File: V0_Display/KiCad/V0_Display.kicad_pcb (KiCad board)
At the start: 2 copper layers, 80 x 35 mm, 31 parts, among them J1 USB_B_Micro, J2 I2C Header 1, J3 Conn_01x03, J4 Conn_01x02, J5 SWD Header, J6 I2C Header 2, J7 USB_Header, J8 Conn_01x02, SW1 SW_SPST, SW2 SW_SPST, SW3 SW_SPST, SW4 SW_SPST, SW5 SW_SPST, SW6 SW_SPST, SW7 Rotary_Encoder_Switch, U1 AP2127K-3.3, U2 STM32F042F6Px, U3 74LVC1G17

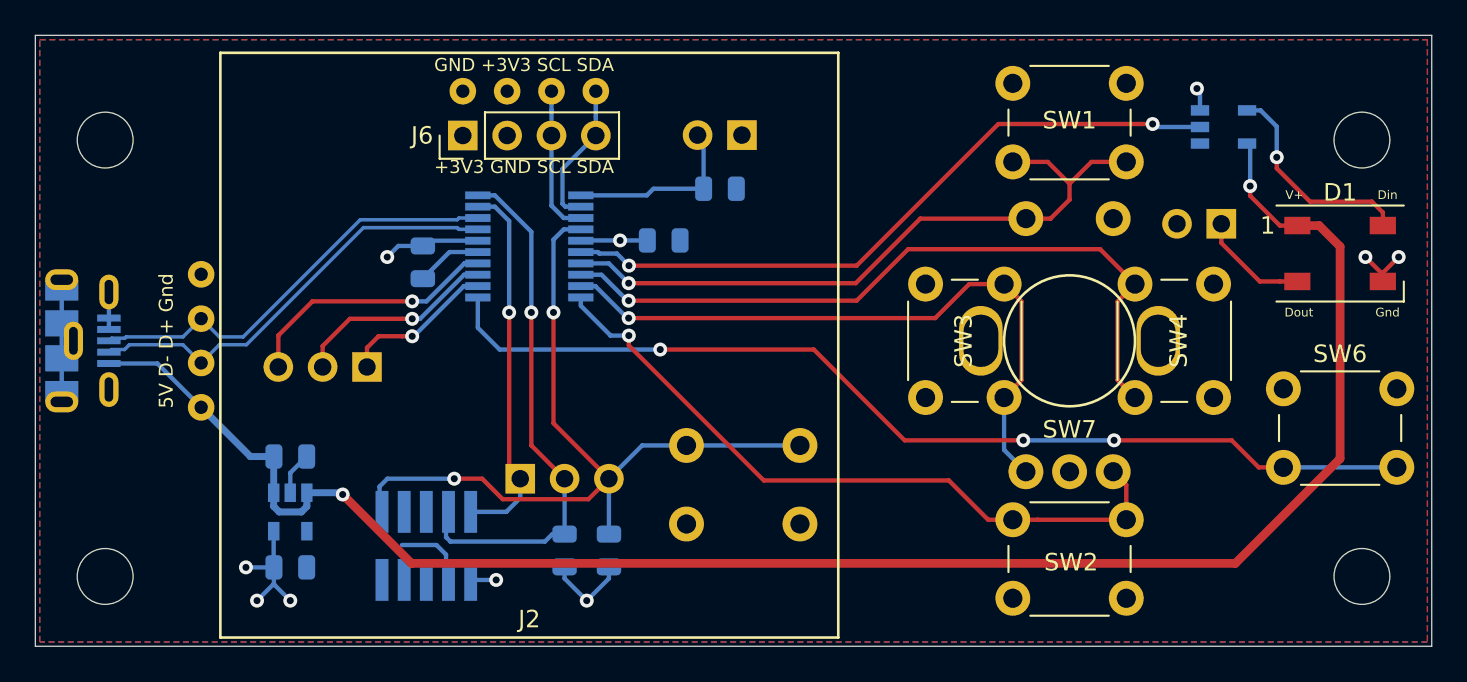
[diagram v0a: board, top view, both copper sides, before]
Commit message: Library Localization and Pinout changes
Added Selection jumpers for pins 1 and 2 on OLED header (Power and Ground) for use with different OLED pinouts.

Moved all footprints, schematic symbols and 3D models to the V0 folder for simplification
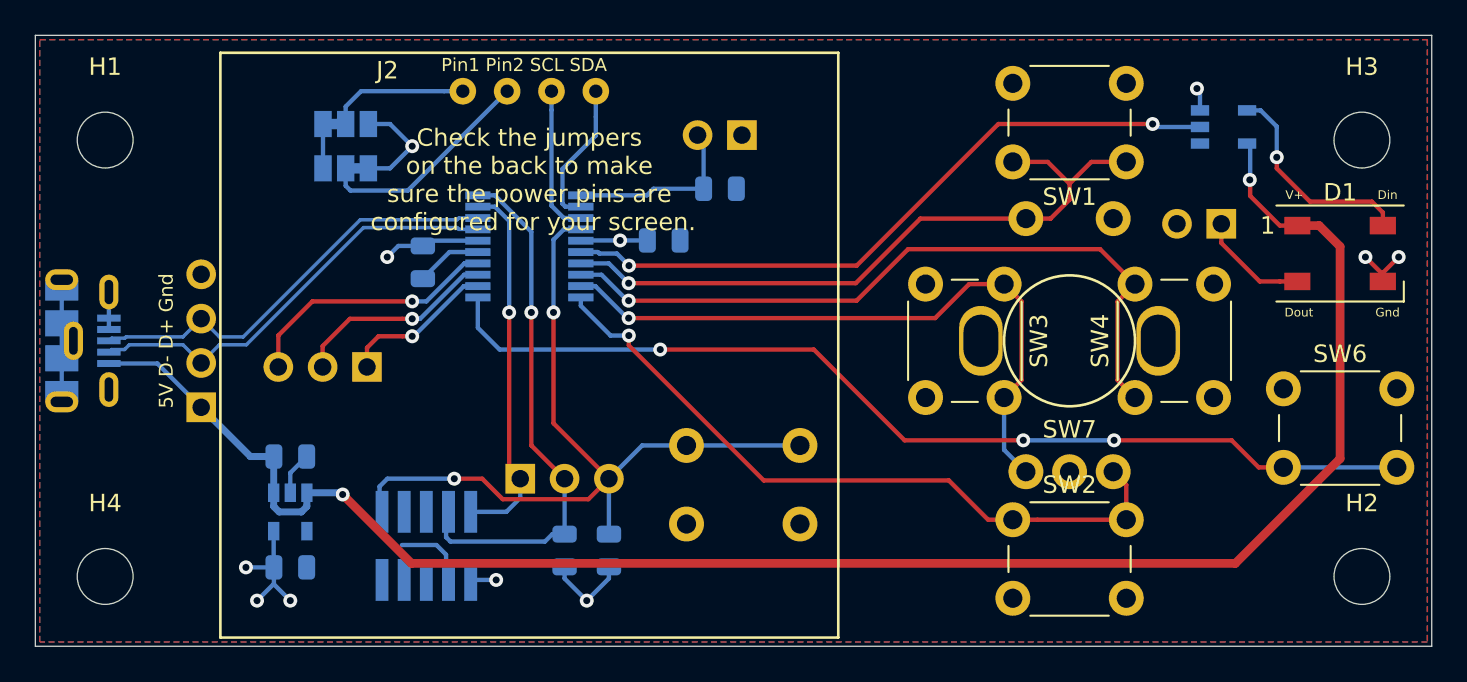
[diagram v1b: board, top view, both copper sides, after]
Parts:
- removed J6: I2C Header 2, Connector_PinHeader_2.54mm:PinHeader_1x04_P2.54mm_Vertical
- added JP1: Pin2, V0-Display:SolderJumper-3_P1.3mm_Bridged12_Pad1.0x1.5mm, B.Cu at (103.0, 57.3)
- added JP2: Pin1, V0-Display:SolderJumper-3_P1.3mm_Bridged12_Pad1.0x1.5mm, B.Cu at (103.0, 54.7)
- C1, C2, C3, C4: footprint Capacitor_SMD:C_0805_2012Metric -> V0-Display:C_0805_2012Metric
- D1: footprint LED_SMD:LED_WS2812B_PLCC4_5.0x5.0mm_P3.2mm -> V0-Display:LED_WS2812B_PLCC4_5.0x5.0mm_P3.2mm
- GPIO1: footprint Connector_PinHeader_2.54mm:PinHeader_1x03_P2.54mm_Horizontal -> V0-Display:PinHeader_1x03_P2.54mm_Vertical
- H1, H2, H3, H4: footprint MountingHole:MountingHole_3.2mm_M3 -> V0-Display:MountingHole_3.2mm_M3
- J1: footprint TRA_KiCad_Footprints:MolexVertical&Horizontal_MicroB -> V0-Display:MolexVertical&Horizontal_MicroB
- J2: footprint TRA_KiCad_Footprints:1pt3in_OLED -> V0-Display:1pt3in_OLED
- J3: footprint Connector_PinHeader_2.54mm:PinHeader_1x03_P2.54mm_Vertical -> V0-Display:PinHeader_1x03_P2.54mm_Vertical
- J4, J8: footprint Connector_PinHeader_2.54mm:PinHeader_1x02_P2.54mm_Vertical -> V0-Display:PinHeader_1x02_P2.54mm_Vertical
- J5: footprint Connector_PinHeader_1.27mm:PinHeader_2x05_P1.27mm_Vertical_SMD -> V0-Display:PinHeader_2x05_P1.27mm_Vertical_SMD
- J7: footprint TRA_KiCad_Footprints:01x04_unpopulated -> V0-Display:PinHeader_1x04_P2.54mm_Vertical
- R1, R2, R3: footprint Resistor_SMD:R_0805_2012Metric -> V0-Display:R_0805_2012Metric
- SW1, SW2, SW3, SW4: footprint Button_Switch_THT:SW_PUSH_6mm_H9.5mm -> V0-Display:SW_PUSH_6mm
- SW5, SW6: footprint Button_Switch_THT:SW_PUSH_6mm -> V0-Display:SW_PUSH_6mm
- SW7: footprint TRA_KiCad_Footprints:EN11_Encoder -> V0-Display:EN11_Encoder
- U1: footprint Package_TO_SOT_SMD:SOT-23-5 -> V0-Display:SOT-23-5
- U2: footprint Package_SO:TSSOP-20_4.4x6.5mm_P0.65mm -> V0-Display:TSSOP-20_4.4x6.5mm_P0.65mm
- U3: footprint digikey-footprints:SOT-753 -> V0-Display:SOT-753
- moved J7 3.81 mm to (94.7, 71.0), turned to 0 degrees
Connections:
- J2 pad 1: GND -> Pin1
- J2 pad 2: +3V3 -> Pin2
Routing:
- net Pin2: track 0.00 -> 12.7 mm
- net Pin1: track 0.00 -> 8.07 mm
- net +3V3: track 23.2 -> 29.3 mm, vias 7 -> 8
- net GND: track 26.2 -> 28.7 mm
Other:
- board text added: "1 2 3 GPIO"
- board text added: "1(GND)"
- board text added: "1(VCC)"
- board text added: "2(GND)"
- board text added: "2(VCC)"
- board text added: "Check the jumpers on the back to make sure the power pins are configured for your screen."
- board text added: "Neo-Out Gnd"
- board text added: "Pin1 Pin2 SCL SDA"
- board text added: "SDA SCL Pin2 Pin1"
- board text removed: "+3V3 GND SCL SDA"
- board text removed: "GND +3V3 SCL SDA"
- board text removed: "GPIO 1 2 3"
- board text removed: "SDA SCL +3V3 GND"
- board text removed: "SDA SCL GND +3V3"

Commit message: Add VORON logo and Rev number
Add Logo and Rev number
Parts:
- added G***: LOGO, V0-Display:VoronLogo_6pt5mm_silkScreen, B.Cu at (144.4, 67.2)
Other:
- board text added: "T. Abraham V0-Display Rev-C"
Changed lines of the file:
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@@
   (general
     (thickness 1.6)
-    (drawings 55)
+    (drawings 56)
     (tracks 280)
     (zones 0)
-    (modules 32)
+    (modules 33)
     (nets 25)
   )
@@
     (solder_mask_min_width 0.25)
     (aux_axis_origin 0 0)
-    (grid_origin 94.67 70.96)
+    (grid_origin 144.42 67.15)
     (visible_elements 7FFFFFFF)
     (pcbplotparams
@@
     (add_net "Net-(D1-Pad2)")
     (add_net "Net-(D1-Pad4)")
-    (add_net "Net-(GPIO1-Pad1)")
-    (add_net "Net-(GPIO1-Pad2)")
-    (add_net "Net-(J5-Pad6)")
-    (add_net "Net-(J5-Pad7)")
-    (add_net "Net-(J5-Pad8)")
-    (add_net "Net-(J5-Pad9)")
-    (add_net "Net-(U1-Pad4)")
     (add_net Pin1)
     (add_net Pin2)
@@
     (add_net VBUS)
     (add_net ~Reset)
+  )
+  (module V0-Display:VoronLogo_6pt5mm_silkScreen (layer B.Cu)
+    (at 144.42 67.15)
+    (fp_text reference G*** (at 0 0) (layer B.SilkS) hide
+      (effects (font (size 1.524 1.524) (thickness 0.3)) (justify mirror))
+    )
+    (fp_text value LOGO (at 0.75 0) (layer B.SilkS) hide
+      (effects (font (size 1.524 1.524) (thickness 0.3)) (justify mirror))
+    )
+    (fp_poly (pts (xy 2.7686 1.64985) (xy 2.7686 -1.649849) (xy 1.379308 -2.450524) (xy 1.039339 -2.646185)
+      (xy 0.729012 -2.824267) (xy 0.458882 -2.978754) (xy 0.239505 -3.10363) (xy 0.081439 -3.192877)
+      (xy -0.004761 -3.240478) (xy -0.017692 -3.24677) (xy -0.061819 -3.221166) (xy -0.183209 -3.150713)
+      (xy -0.371255 -3.041566) (xy -0.615351 -2.899881) (xy -0.904891 -2.731815) (xy -1.229269 -2.543525)
+      (xy -1.397 -2.446162) (xy -2.622352 -1.734876) (xy -1.566334 -1.734876) (xy -1.527559 -1.754402)
+      (xy -1.409521 -1.769187) (xy -1.234533 -1.776891) (xy -1.159934 -1.777479) (xy -0.7366 -1.776959)
+      (xy -0.722179 -1.755076) (xy 0 -1.755076) (xy 0.04685 -1.765563) (xy 0.171616 -1.7735)
+      (xy 0.350623 -1.777596) (xy 0.4191 -1.777886) (xy 0.8382 -1.777772) (xy 1.3208 -1.034043)
+      (xy 1.485838 -0.779678) (xy 1.637963 -0.545166) (xy 1.765863 -0.347951) (xy 1.858223 -0.205476)
+      (xy 1.897288 -0.145156) (xy 1.991177 0) (xy 1.129093 0) (xy 0.564546 -0.866076)
+      (xy 0.394034 -1.128735) (xy 0.244186 -1.361619) (xy 0.123286 -1.551683) (xy 0.039618 -1.685882)
+      (xy 0.001465 -1.751172) (xy 0 -1.755076) (xy -0.722179 -1.755076) (xy 0.4064 -0.042603)
+      (xy 0.654036 0.333568) (xy 0.884037 0.683745) (xy 1.09042 0.998762) (xy 1.267202 1.269449)
+      (xy 1.408399 1.486639) (xy 1.508029 1.641163) (xy 1.560108 1.723852) (xy 1.566333 1.734877)
+      (xy 1.527558 1.754403) (xy 1.40952 1.769188) (xy 1.234532 1.776892) (xy 1.159933 1.77748)
+      (xy 0.7366 1.77696) (xy -0.4064 0.042604) (xy -0.654037 -0.333567) (xy -0.884038 -0.683744)
+      (xy -1.090421 -0.998761) (xy -1.267203 -1.269448) (xy -1.4084 -1.486638) (xy -1.50803 -1.641162)
+      (xy -1.560109 -1.723851) (xy -1.566334 -1.734876) (xy -2.622352 -1.734876) (xy -2.7686 -1.649983)
+      (xy -2.7686 0) (xy -1.991178 0) (xy -1.129094 0) (xy -0.564547 0.866077)
+      (xy -0.394035 1.128736) (xy -0.244187 1.36162) (xy -0.123287 1.551684) (xy -0.039619 1.685883)
+      (xy -0.001466 1.751173) (xy 0 1.755077) (xy -0.046851 1.765564) (xy -0.171617 1.773501)
+      (xy -0.350624 1.777597) (xy -0.4191 1.777887) (xy -0.8382 1.777773) (xy -1.3208 1.034044)
+      (xy -1.485839 0.779679) (xy -1.637964 0.545167) (xy -1.765864 0.347952) (xy -1.858224 0.205477)
+      (xy -1.897289 0.145157) (xy -1.991178 0) (xy -2.7686 0) (xy -2.7686 1.64985)
+      (xy 0 3.245448) (xy 2.7686 1.64985)) (layer B.SilkS) (width 0.01))
   )
   (module V0-Display:LED_WS2812B_PLCC4_5.0x5.0mm_P3.2mm (layer F.Cu)
@@
     (descr https://www.omron.com/ecb/products/pdf/en-b3f.pdf)
     (tags "tact sw push 6mm")
-    (fp_text reference SW5 (at 3.25 2) (layer B.SilkS)
+    (fp_text reference SW5 (at -2.999 -2.387) (layer B.SilkS)
       (effects (font (size 1 1) (thickness 0.15)) (justify mirror))
     )
@@
     (tags resistor)
     (attr smd)
-    (fp_text reference R2 (at 0 1.65) (layer B.SilkS)
+    (fp_text reference R2 (at 2.756 0.076) (layer B.SilkS)
       (effects (font (size 1 1) (thickness 0.15)) (justify mirror))
     )
@@
     (tags capacitor)
     (attr smd)
-    (fp_text reference C4 (at 0 1.65) (layer B.SilkS)
+    (fp_text reference C4 (at 2.93 -0.092) (layer B.SilkS)
       (effects (font (size 1 1) (thickness 0.15)) (justify mirror))
     )
@@
     )
   )
+  (gr_text "T. Abraham\nV0-Display\nRev-C" (at 127.148 66.134) (layer B.SilkS)
+    (effects (font (size 1.5 1.5) (thickness 0.2)) (justify mirror))
+  )
   (gr_text "Neo-Out Gnd\n" (at 152.205 58.565) (layer B.SilkS)

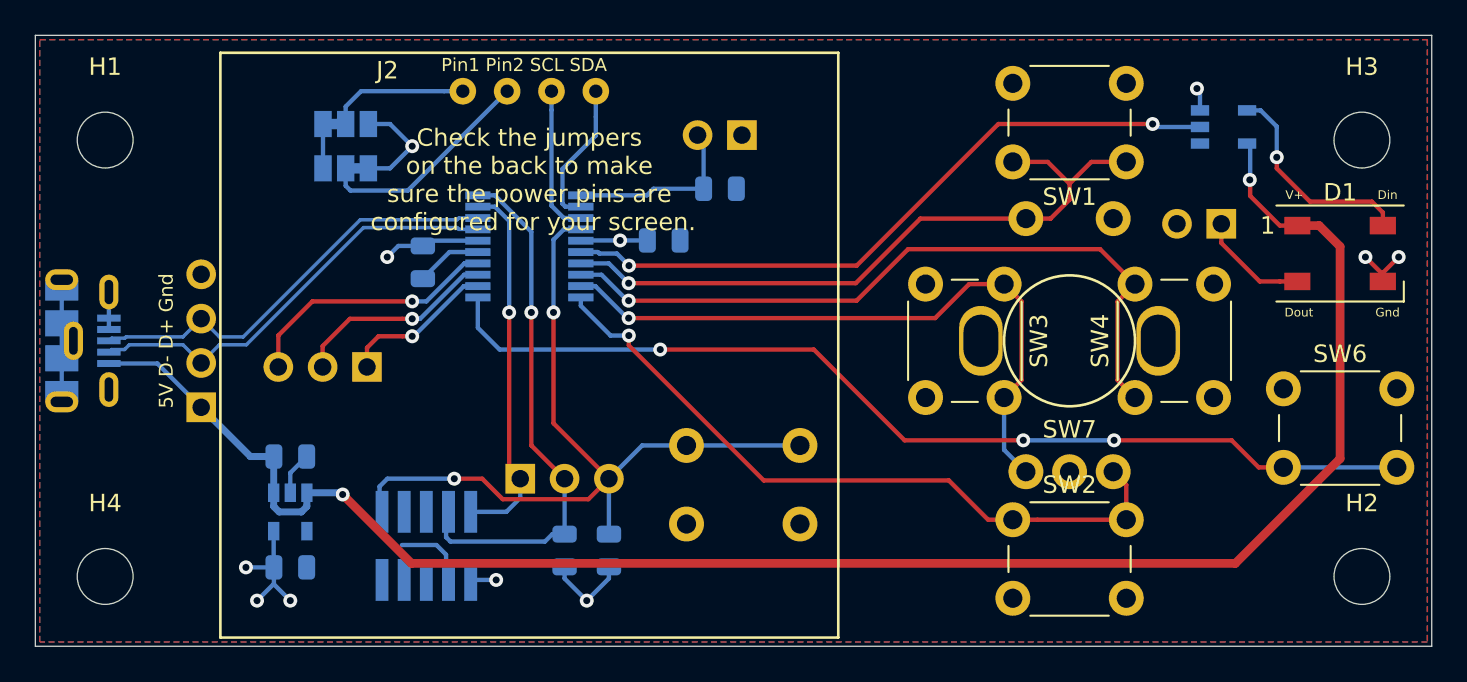
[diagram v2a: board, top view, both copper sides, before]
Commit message: Removal of control buttons
No-one used them, why have them on the board?
Removed 4 directional buttons
Updates of documentation
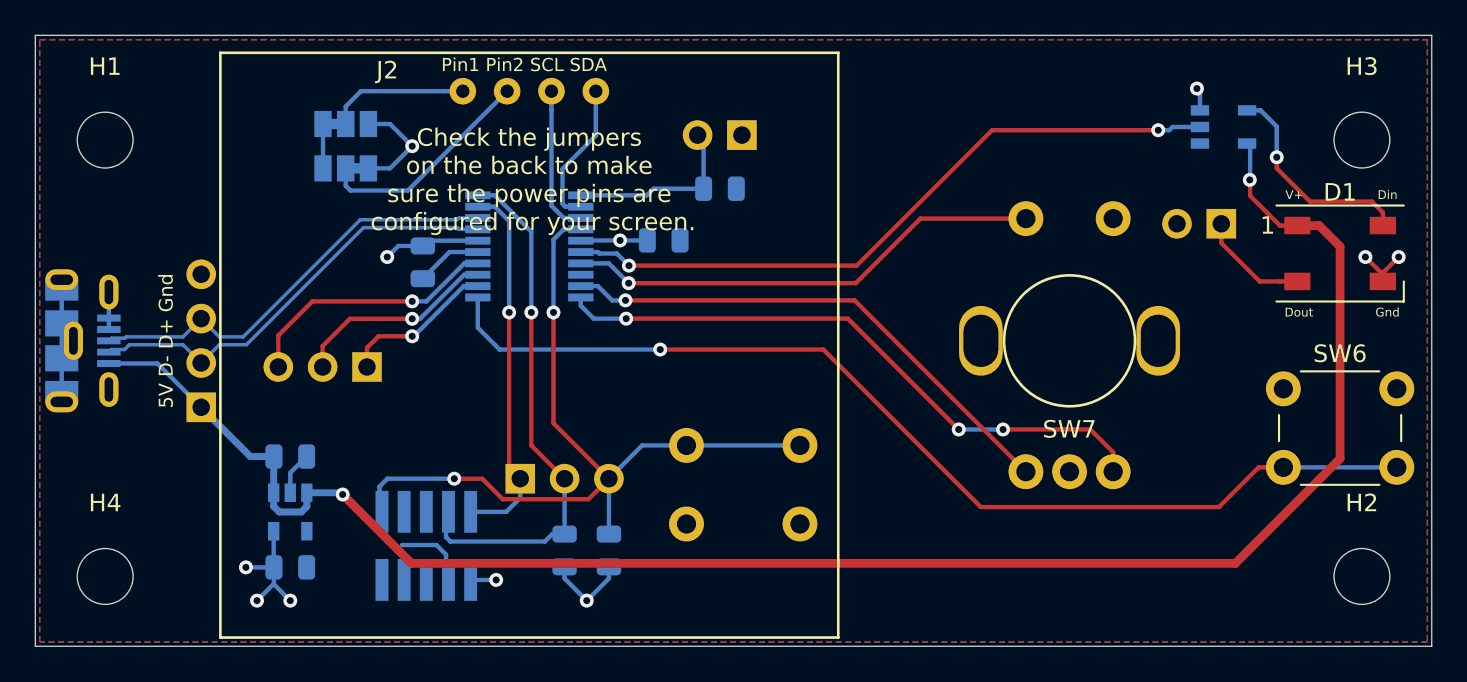
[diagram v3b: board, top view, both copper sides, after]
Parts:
- removed G***: LOGO, V0-Display:VoronLogo_6pt5mm_silkScreen
- removed SW1, SW2, SW3, SW4: SW_SPST, V0-Display:SW_PUSH_6mm
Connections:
- net Button_Down renamed Encoder_B
- net Button_Left renamed Encoder_A
- net Button_Up renamed Encoder_Switch
- U2 pad 8: Button_Right -> (no net)
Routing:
- net Button_Right: track 41.7 -> 0.00 mm, vias 1 -> 0
- net Encoder_Switch: track 38.9 -> 27.5 mm
- net Encoder_A: track 38.6 -> 29.9 mm
- net Encoder_B: track 40.2 -> 35.6 mm, vias 1 -> 3
- net Kill_Switch: track 57.7 -> 59.6 mm, vias 3 -> 1
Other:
- board text added: "T. Abraham V0-Display Rev-D"
- board text removed: "T. Abraham V0-Display Rev-C"
